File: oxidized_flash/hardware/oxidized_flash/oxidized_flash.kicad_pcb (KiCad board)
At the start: 2 copper layers, 61 x 21.6 mm, 21 parts, among them J1 USB_A, J2 Conn_ARM_JTAG_SWD_10, U1 LM1117-3.3, U2 ATSAMD51G19A-MU, U3 MT25QL

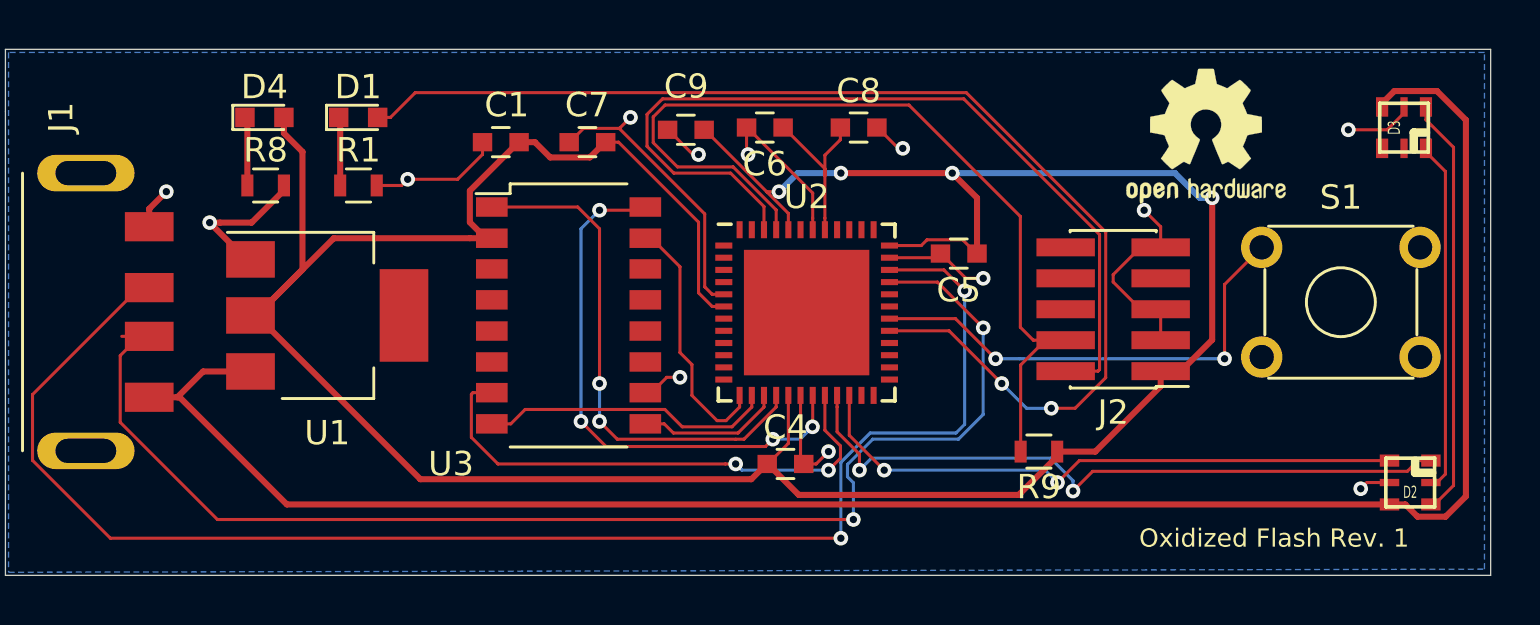
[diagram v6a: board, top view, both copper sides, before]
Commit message: Update APA and flash footprints
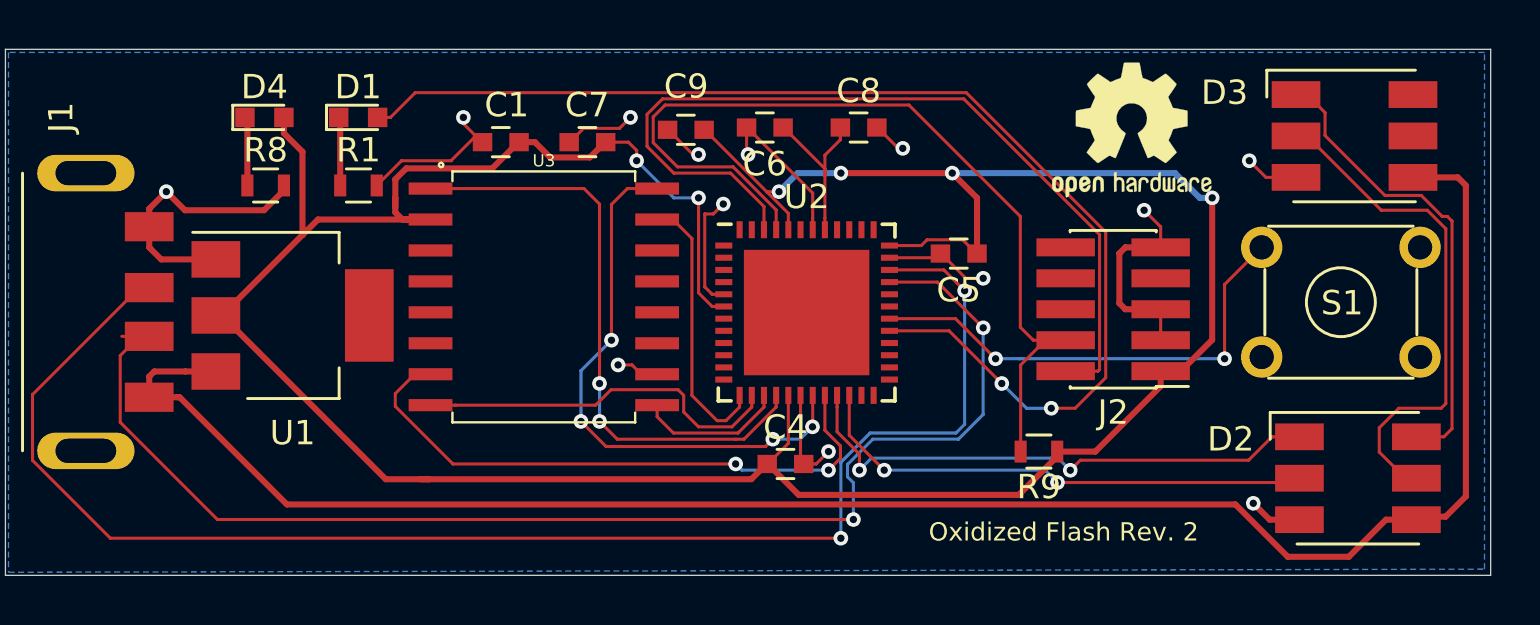
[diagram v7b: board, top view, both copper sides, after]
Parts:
- D2, D3: footprint Custom_LED:APA102-2020 -> Custom_LED:LED_RGB_5050-6
- U3: footprint Housings_SSOP:SOP-16_4.4x10.4mm_Pitch1.27mm -> Custom_IC:SOP2-16
- moved REF*** 3.06 mm to (70.4, 23.6)
- moved D2 2.15 mm to (79.6, 37.9)
- moved D3 2.06 mm to (79.5, 23.9), turned to 0 degrees
- moved U1 1.42 mm to (35.9, 31.2)
- moved U3 1.27 mm to (46.2, 30.5), turned to 270 degrees
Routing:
- net /MOSI: track 28.4 -> 22.5 mm
- net Net-(D2-Pad6): track 14.4 -> 19.2 mm
- net Net-(D2-Pad5): track 17.3 -> 21.3 mm
- net /SCK: track 25.0 -> 21.0 mm
- net Net-(U2-Pad16): track 21.3 -> 24.7 mm
- net Net-(U2-Pad20): track 21.4 -> 24.7 mm
- net Net-(U2-Pad14): track 12.0 -> 15.3 mm
- net +5V: track 79.6 -> 77.0 mm
- net +3V3: track 126.3 -> 128.4 mm, vias 4 -> 6
- net GND: track 57.0 -> 58.9 mm
- net Net-(U2-Pad13): track 10.5 -> 11.3 mm
- net Net-(U2-Pad19): track 22.5 -> 23.1 mm
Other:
- board text added: "Oxidized Flash Rev. 2"
- board text removed: "Oxidized Flash Rev. 1"
